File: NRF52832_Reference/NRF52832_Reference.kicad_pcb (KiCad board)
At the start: 2 copper layers, 95 x 50 mm, 107 parts, among them J1 Conn_01x10_Male, J10 Conn_01x10_Male, J11 Conn_01x04_Male, J12 SWD_Header, J16 MM8130-2600RA2, J17 USB_B_Micro, J18 Conn_01x02_Male, J2 Conn_01x10_Male, J3 Conn_01x02_Male, J4 Conn_01x02_Male, J5 Conn_01x02_Male, J6 Conn_01x02_Male, J7 Conn_01x02_Male, SW1 Button, SW2 Button, U1 SLIDE_SW_DPDT, U10 DW01, U11 LMV331ICT, U12 AP2138N-3.0TRG1, U13 FS8205A, U14 SLIDE_SW_DPDT, U2 AT34C04-X5M-T, U3 NHD-C12832A1Z-NSW-BBW-3V3, U4 LTR-329ALS-01, U5 TCN75AVUA713, U6 nRF52832, U7 TPS613222ADBVR, U8 NCV8161BSN330T1G, U9 TP4056E-SN2L1P, Y1 32.768kHz, Y2 32MHz

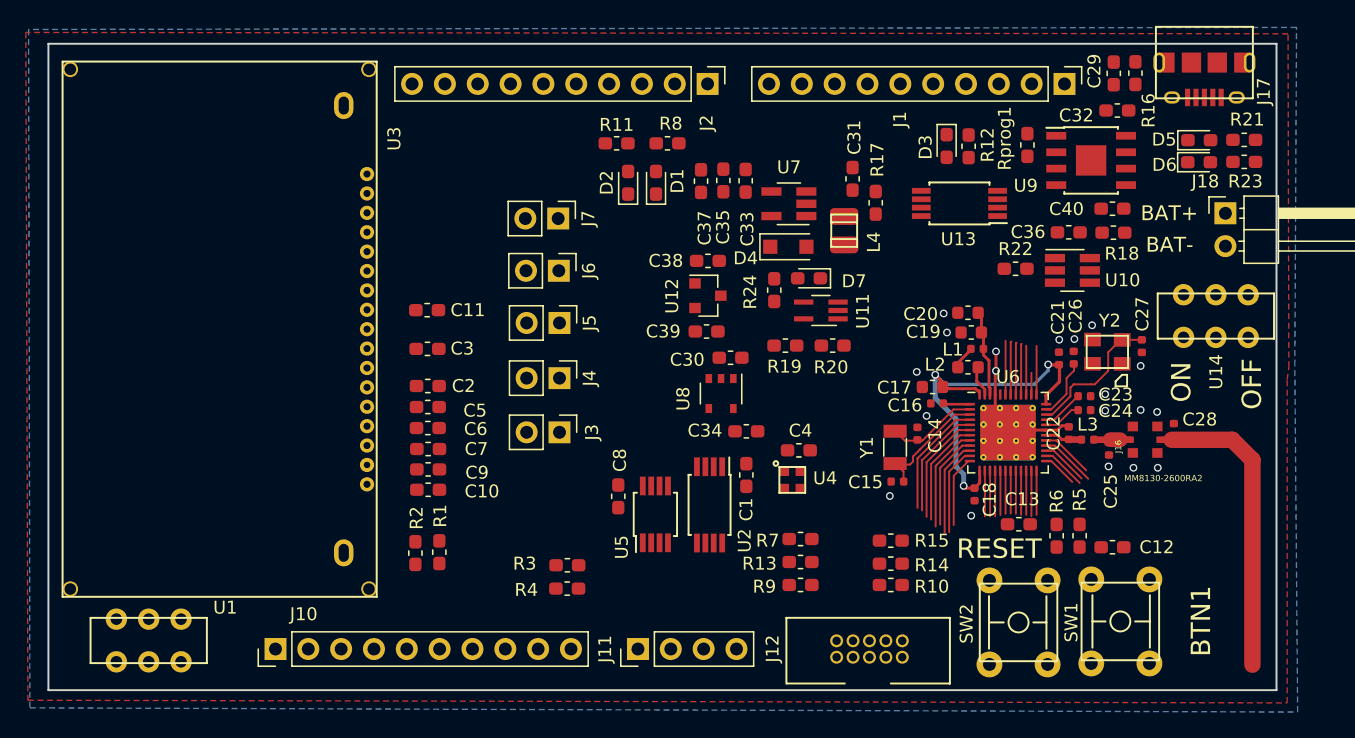
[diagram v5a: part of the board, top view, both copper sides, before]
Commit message: Finished routing of components. Silkscreen labels still not finished.
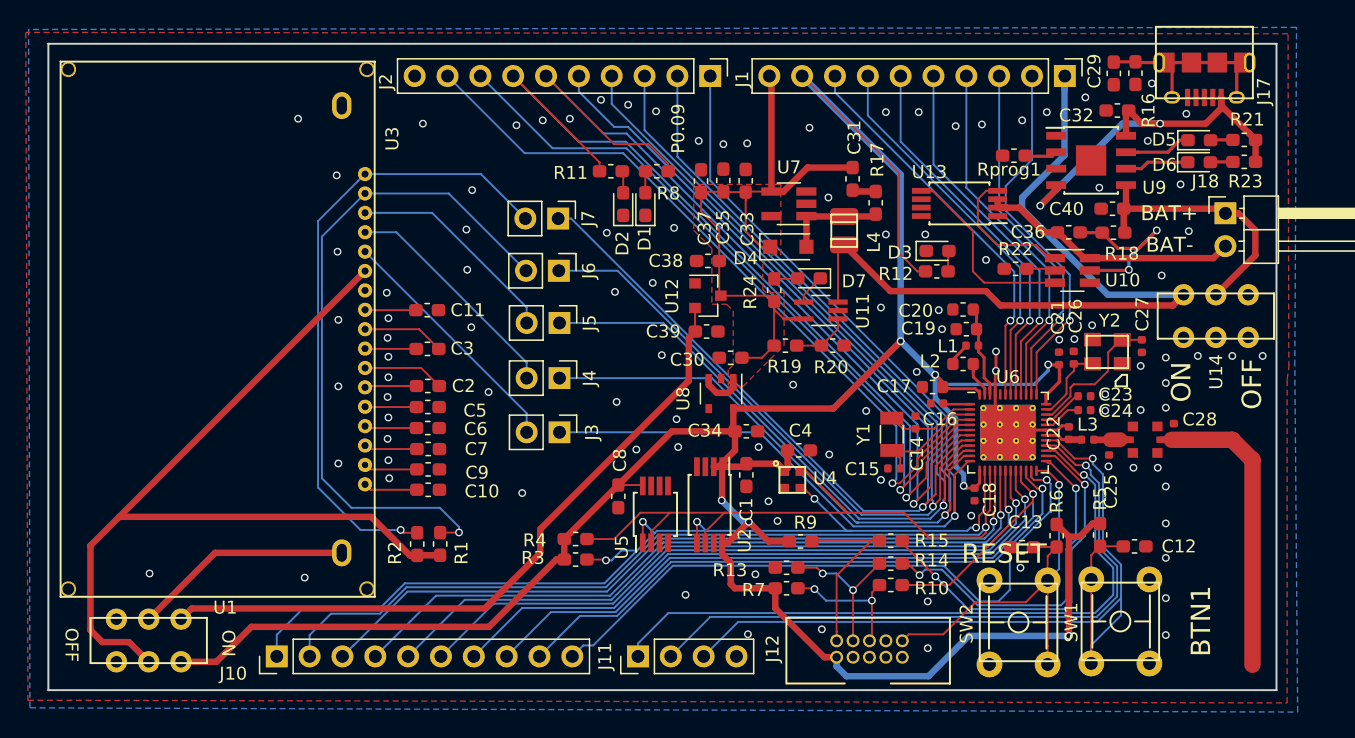
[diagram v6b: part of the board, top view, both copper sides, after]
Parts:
- moved R12 9.99 mm to (162.4, 91.7), turned to 0 degrees
- moved D3 8.15 mm to (162.5, 90.1), turned to 0 degrees
- moved R7 3.96 mm to (150.8, 116.2)
- moved R4 3.89 mm to (134.5, 112.4)
- moved R9 3.37 mm to (151.9, 112.6)
- moved R8 2.31 mm to (140.8, 83.9)
- moved R11 2.20 mm to (137.2, 83.9)
- moved D1 1.85 mm to (139.9, 86.5)
- moved C13 1.80 mm to (169.0, 113.0)
- moved C12 1.72 mm to (177.7, 113.0)
- moved D2 1.69 mm to (138.2, 86.5)
- moved R5 1.59 mm to (175.1, 112.1)
- moved Rprog1 1.33 mm to (168.4, 82.7), turned to 180 degrees
- moved R13 1.17 mm to (150.8, 114.6)
- moved C15 1.05 mm to (159.1, 106.9)
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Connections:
- J1 pad 10: P0.31 -> 5V_Ref
- J1 pad 2: 5V_Ref -> P0.25
- J1 pad 3: 3V3_Ref -> P0.26
- J1 pad 4: P0.25 -> P0.27
- J1 pad 5: P0.26 -> P0.28
- J1 pad 6: P0.27 -> P0.29
- J1 pad 7: P0.28 -> P0.30
- J1 pad 8: P0.29 -> P0.31
- J1 pad 9: P0.30 -> 3V3_Ref
- J2 pad 1: P0.02 -> P0.10_SI
- J2 pad 2: P0.03 -> P0.09_SCL
- J2 pad 3: P0.04 -> P0.08_A0
- J2 pad 4: P0.05 -> P0.07_RES
- J2 pad 6: P0.07_RES -> P0.05
- J2 pad 7: P0.08_A0 -> P0.04
- J2 pad 8: P0.09_SCL -> P0.03
- J2 pad 9: P0.10_SI -> P0.02
- R11 pad 1: P0.22 -> P0.04
- R13 pad 1: /Sheet5BF15571/SWDCLK -> Net-(J12-Pad4)
- R8 pad 1: P0.23 -> P0.05
- U1 pad 1: 3V_Ref -> Net-(U1-Pad1)
- U1 pad 2: Net-(U1-Pad2) -> Net-(R1-Pad1)
- U1 pad 3: Net-(U1-Pad3) -> 3V3_Ref
- U1 pad 4: 3V3_Ref -> Net-(U1-Pad4)
- U1 pad 5: Net-(R1-Pad1) -> Net-(U1-Pad5)
- U1 pad 6: Net-(U1-Pad6) -> 3V_Ref
- U3 pad 18: Net-(U1-Pad2) -> Net-(U1-Pad5)
- U6 pad 49: (no net) -> GND
- U9 pad 9: (no net) -> GND
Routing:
- net 3V3_Ref: track 30.9 -> 217.3 mm, vias 3 -> 7
- net P0.12_SCL: track 3.61 -> 106.2 mm, vias 0 -> 1
- net P0.06_CS1: track 8.25 -> 90.2 mm, vias 0 -> 1
- net P0.07_RES: track 7.51 -> 87.2 mm, vias 0 -> 1
- net P0.08_A0: track 7.63 -> 84.8 mm, vias 0 -> 1
- net P0.09_SCL: track 6.89 -> 83.8 mm, vias 0 -> 1
- net P0.11_SDA: track 3.61 -> 79.0 mm, vias 0 -> 5
- net P0.10_SI: track 5.63 -> 80.8 mm, vias 0 -> 1
- net Net-(R1-Pad1): track 0.00 -> 68.2 mm
- net P0.24: track 4.14 -> 67.6 mm, vias 0 -> 1
- net V+: track 0.00 -> 60.4 mm
- net P0.18_SWO: track 3.50 -> 62.6 mm, vias 0 -> 1
- net P0.05: track 8.31 -> 66.7 mm, vias 0 -> 1
- net P0.04: track 8.71 -> 65.6 mm, vias 0 -> 1
- net P0.13: track 3.61 -> 59.0 mm, vias 0 -> 1
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- added copper zone on F.Cu, net 5V_Ref
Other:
- board text added: "P0.09"

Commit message: Finished adding silkscreen labels. Added 3 M2 mounting holes. Generated gerber files.
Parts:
- added M1: MountingHole_2.2mm_M2, MountingHole:MountingHole_2.2mm_M2, F.Cu at (124.1, 85.8)
- added M2: MountingHole_2.2mm_M2, MountingHole:MountingHole_2.2mm_M2, F.Cu at (129.0, 110.0)
- added M3: MountingHole_2.2mm_M2, MountingHole:MountingHole_2.2mm_M2, F.Cu at (153.7, 102.8)
- moved C13 2.88 mm to (171.0, 110.9)
- moved R6 1.81 mm to (173.5, 111.8), turned to 90 degrees
- moved Rprog 1.53 mm to (169.5, 83.8), turned to 270 degrees
- moved C4 0.74 mm to (151.5, 106.2)
- moved U4 0.65 mm to (151.1, 108.5)
- moved R5 0.26 mm to (175.1, 111.8), turned to 90 degrees
- renumbered Rprog1 to Rprog
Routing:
- net 3V3_Ref: track 217.3 -> 214.4 mm
- net Net-(J7-Pad2): track 48.7 -> 50.7 mm
- net RESET: track 34.4 -> 36.4 mm
- net P0.24: track 67.6 -> 69.3 mm
- net P0.12_SCL: track 106.2 -> 105.5 mm
- net GND: vias 104 -> 113
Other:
- net class nrf_ref_track removed
- rule pad_to_mask_clearance: 0.2 -> 0.15
- board text added: "5V"
- board text added: "Custom NRF52832 Board V1.0"
- board text added: "GND"
- board text added: "I2C"
- board text added: "LCD"
- board text added: "P0.02"
- board text added: "P0.03"
- board text added: "P0.04"
- board text added: "P0.05"
- board text added: "P0.06"
- board text added: "P0.06 - /CS1"
- board text added: "P0.07"
- board text added: "P0.07 - /RST"
- board text added: "P0.08"
- board text added: "P0.08 - A0"
- board text added: "P0.09 - SCL"
- board text added: "P0.10"
- board text added: "P0.10 - SI"
- board text added: "P0.11 - SDA"
- board text added: "P0.12 - SCL"
- board text added: "P0.13"
- board text added: "P0.14"
- board text added: "P0.15"
- board text added: "P0.16"
- board text added: "P0.17"
- board text added: "P0.18"
- board text added: "P0.19"
- board text added: "P0.20"
- board text added: "P0.22"
- board text added: "P0.23"
- board text added: "P0.24"
- board text added: "P0.25"
- board text added: "P0.26"
- board text added: "P0.27"
- board text added: "P0.28"
- board text added: "P0.29"
- board text added: "P0.30"
- board text added: "P0.31"
- board text added: "SCL/P0.12"
- board text added: "SDA/P0.11"
- board text added: "SWD Interface"
- board text added: "Temp Sensor Photo Sensor EEPROM 4KB"
- board text added: "V+"
- board text added: "VCC"
